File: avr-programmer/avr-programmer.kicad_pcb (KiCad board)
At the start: 2 copper layers, 34.3 x 16.5 mm, 11 parts, among them J1 FTDI, J2 ISP-2560, U1 ATMEGA328, X1 16MHz 18pF

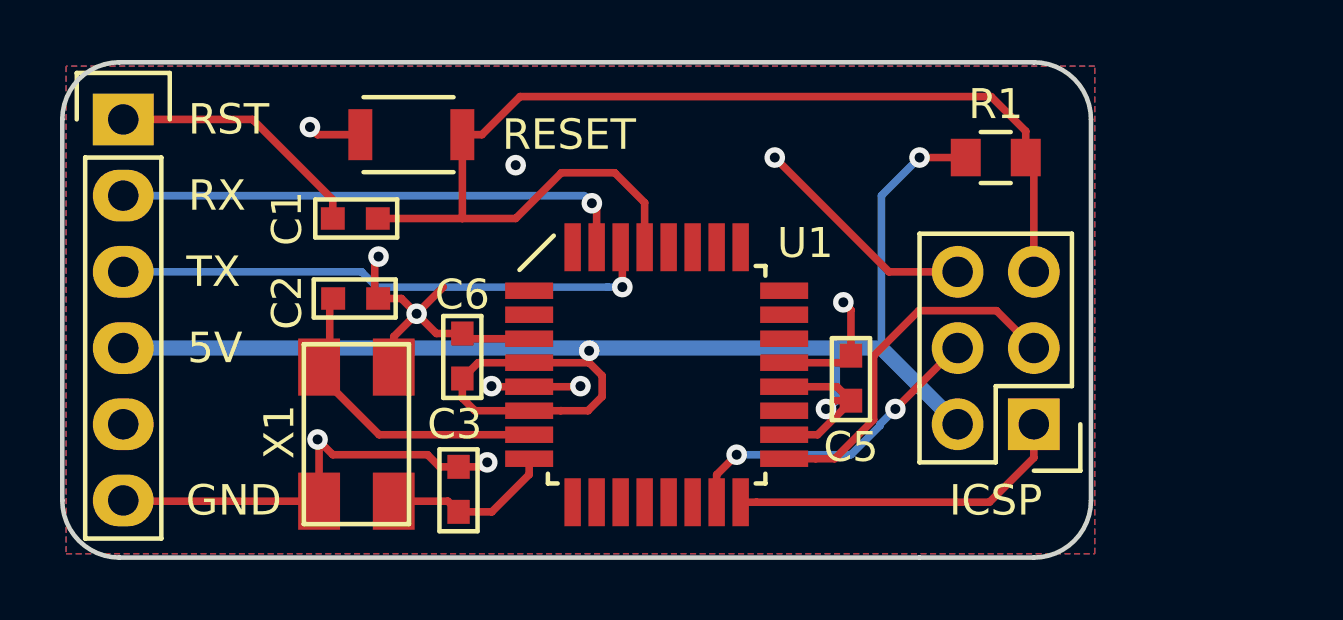
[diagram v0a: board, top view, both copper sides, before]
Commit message: Add switch to AVR Programmer v1.1
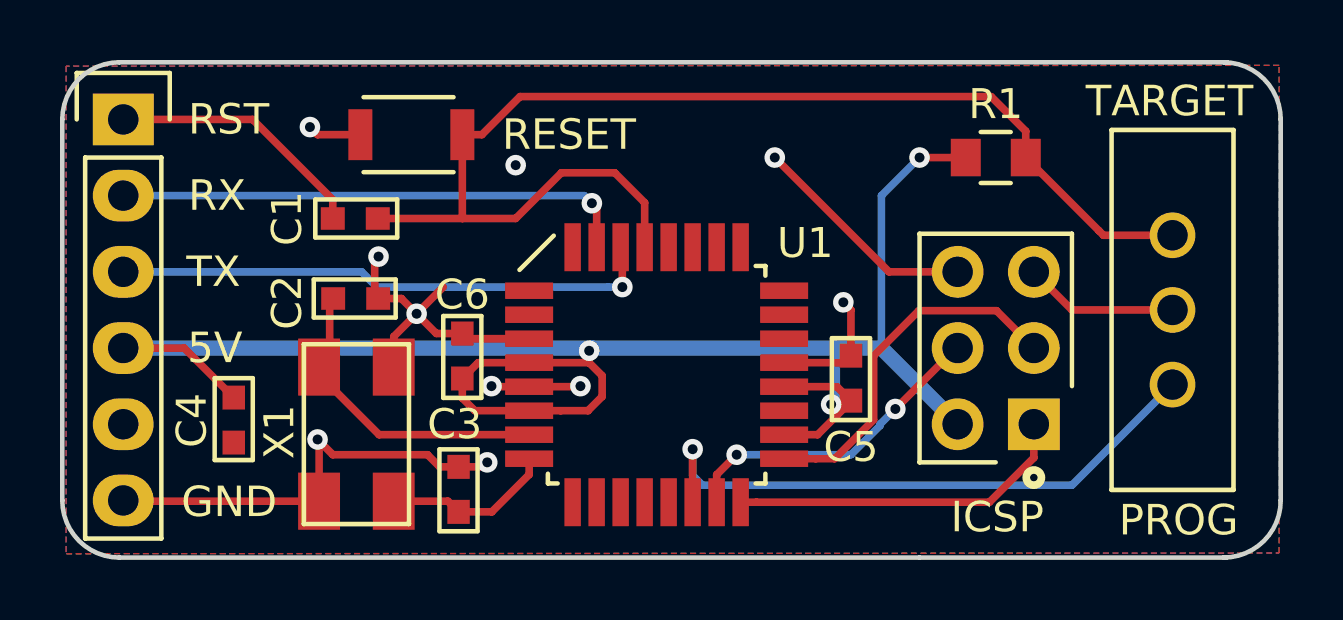
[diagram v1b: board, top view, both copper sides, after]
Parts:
- added C4: 1uF, Wickerlib:RLC-0603-SMD, F.Cu at (106.7, 87.5)
- added S2: SLIDE, Wickerlib:SWITCH-ESWITCH-SLIDE-TH-EG1218, F.Cu at (138.0, 83.8)
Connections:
- net +5V renamed VIN
- J2 pad 5: /~RESET -> /ISP_RST
- U1 pad 14: (no net) -> CS_D10
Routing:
- net CS_D10: track 0.00 -> 20.2 mm, vias 0 -> 1
- net /ISP_RST: track 0.00 -> 5.15 mm
- net VIN: track 57.5 -> 61.6 mm
- net /~RESET: track 38.8 -> 41.2 mm
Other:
- board size 34.3 x 16.5 mm -> 40.6 x 16.5 mm
- board text added: "AVR Programmer v1.1"
- board text added: "Assembly Diagram AVR Programmer v1.1 2/9/17"
- board text added: "PROG"
- board text added: "PROG = Put bootloader on other board"
- board text added: "TARGET"
- board text added: "TARGET = Put bootloader on this board"
- board text removed: "1/9/17"
- board text removed: "AVR Programmer v1.0"

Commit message: Fix OSH Park preview issue.
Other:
- rule pad_to_mask_clearance: 0.0762 -> 0.0508
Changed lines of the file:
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@@
     (links 37)
     (no_connects 0)
-    (area 99.338 69.5452 178.510001 123.265001)
+    (area 99.338 69.5198 178.510001 123.265001)
     (thickness 1.6)
     (drawings 49)
@@
     (pad_size 1.524 1.524)
     (pad_drill 0.762)
-    (pad_to_mask_clearance 0.0762)
+    (pad_to_mask_clearance 0.0508)
     (solder_mask_min_width 0.1016)
     (pad_to_paste_clearance -0.0762)
